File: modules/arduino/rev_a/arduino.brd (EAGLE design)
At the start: 67.3 x 66.7 mm, 45 parts, among them IC5 ATMEGA328P-20MU, J1 MODULE_GENERIC, J4 MICRO_USB_B_HIROSE_ZX62-B-5PA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, U3 ATMEGA8U2-MU, Y1 12 MHz, Y2 16MHz

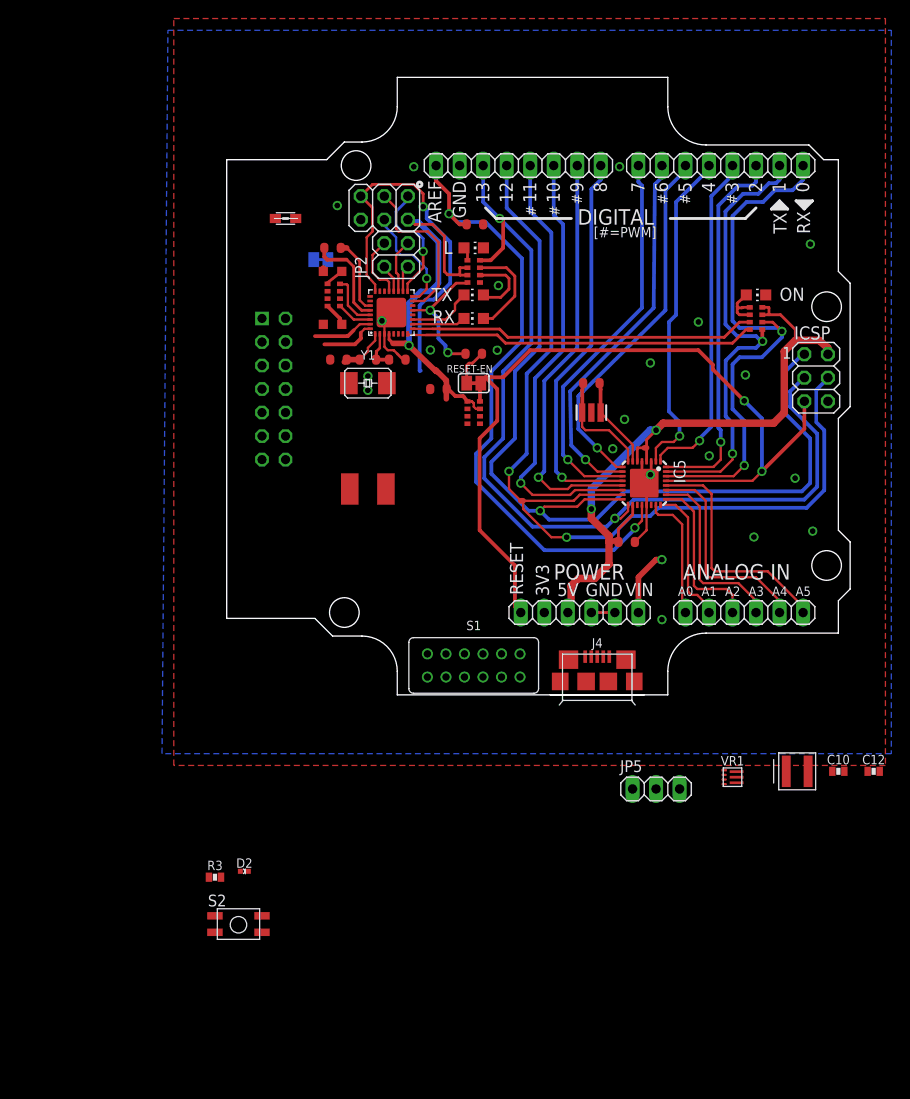
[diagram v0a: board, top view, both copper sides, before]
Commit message: Ardunio WIP
 - Add actual holes for signpost module mounts
 - Replace pin header with switch for IO voltage
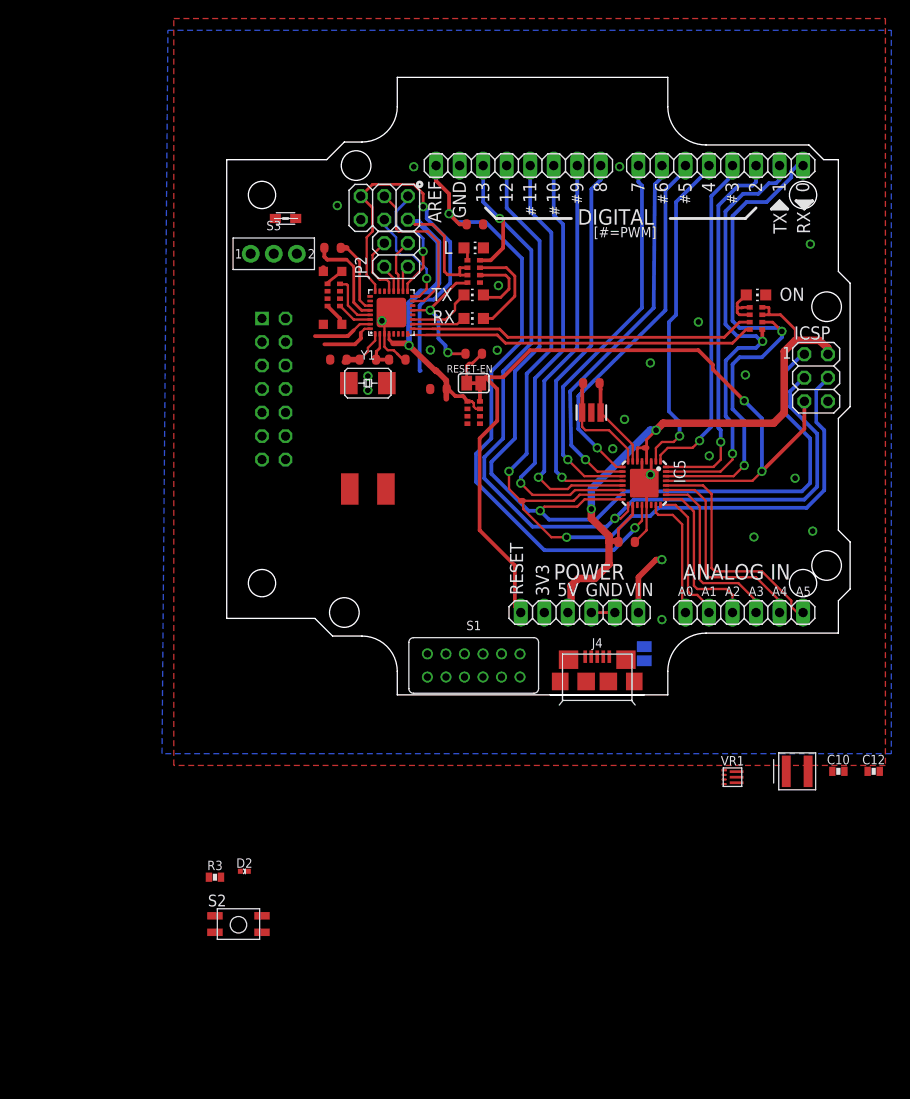
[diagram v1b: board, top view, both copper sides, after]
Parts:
- removed JP5: (no value), pinhead:1X03
- added S3: TE_SSA12/SPDT, switches:TE_SSA12/SPDT
- moved GROUND 55.0 mm to (46.4, -1.91), turned to 270 degrees
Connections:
- net +3V3: no longer JP5.3
- net +5V: now also S3.2
- net MOD_5V: no longer JP5.1
- net MOD_VCCIO: no longer JP5.2
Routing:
- net GND: track 22.2 -> 20.8 mm
- net IO0: track 58.0 -> 57.4 mm

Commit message: Not pretty but it's something
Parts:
- removed L1: BLM21, wuerth-elektronik:0805
- removed Z1, Z2: PGB1010604, varistor:CT/CN0603
- added D1: DIODE, passives:0402_DIODE
- added J2: (no value), jumper:SJ
- added LOGO1: UMICH_SOLID_MEDIUM, logos:UMICH_SOLID_200MIL
- moved C12 55.1 mm to (21.0, 8.26), turned to 270 degrees
- moved C10 54.2 mm to (18.4, 8.89)
- moved L2 51.7 mm to (19.4, 13.3)
- moved S2 50.3 mm to (32.4, 9.40), turned to 270 degrees
- moved VR1 42.9 mm to (18.4, 5.71), turned to 90 degrees
- moved D2 41.1 mm to (36.2, -0.95), turned to 90 degrees
- moved R3 34.3 mm to (19.1, 2.54)
- moved S3 29.2 mm to (6.35, 12.1)
- moved C8 4.51 mm to (15.1, 38.1)
- moved RN3 3.89 mm to (16.4, 35.2)
- moved C11 3.81 mm to (23.5, 29.8)
- moved C9 3.81 mm to (17.1, 29.8)
- moved R1 3.81 mm to (20.3, 29.8)
- moved Y1 3.81 mm to (20.3, 27.3)
- moved GROUND 2.69 mm to (48.3, 0.00), turned to 90 degrees
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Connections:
- net N$7 renamed VR_IND_SW
- removed net USHIELD: L1.2, Z1.2, Z2.2
- net +3V3: now also S3.1
- net +5V: now also C10.1, D1.CATHODE, VR1.1, VR1.7
- net ARD_USB_D+: now also RN3.7; no longer RN3.5, Z1.1
- net ARD_USB_D-: no longer Z2.1
- net ARD_USB_GND: no longer GROUND.2, L1.1
- net ARD_USB_VBUS: no longer D2.ANODE
- net EXT_USB_GND: now also GROUND.1
- net EXT_USB_VBUS: now also D2.ANODE
- net GND: now also GROUND.2; no longer GROUND.1
- net MOD_5V: now also D1.ANODE; no longer C10.1, VR1.1, VR1.7
- net MOD_IN: now also J2.1
- net MOD_VCCIO: now also S3.IN
- net RD+: now also RN3.2; no longer RN3.4
- net RESET: now also J2.2
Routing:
- net +5V: track 123.6 -> 192.8 mm, vias 3 -> 6
- net MOD_USB_VBUS: track 0.00 -> 53.1 mm
- net MOD_USB_D-: track 0.00 -> 51.7 mm
- net +3V3: track 0.00 -> 51.4 mm, vias 0 -> 1
- net ARD_USB_GND: track 10.5 -> 61.0 mm
- net MOD_USB_D+: track 0.00 -> 49.6 mm
- net ARD_USB_D-: track 2.56 -> 51.3 mm, vias 0 -> 1
- net ARD_USB_D+: track 2.14 -> 48.6 mm
- net ARD_USB_VBUS: track 0.00 -> 38.5 mm, vias 0 -> 3
- net EXT_USB_D-: track 0.00 -> 22.8 mm
- net MOD_VCCIO: track 0.00 -> 21.3 mm
- net EXT_USB_VBUS: track 0.00 -> 19.8 mm, vias 0 -> 2
- net USBVCC: track 6.49 -> 25.6 mm, vias 0 -> 2
- net EXT_USB_D+: track 0.00 -> 17.6 mm, vias 0 -> 1
- net RESET: track 98.4 -> 114.2 mm, vias 2 -> 6
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- added copper zone on layer 1, net +3V3
- added copper zone on layer 1, net +5V
- added copper zone on layer 16, net EXT_USB_GND
- added copper zone on layer 1, net VR_IND_SW
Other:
- outline, holes or cut-outs redrawn
- board text added: "2016-08-24"
- board text added: "Pat Pannuto"
- board text added: "Rev A"
- board text added: "Seinduino"

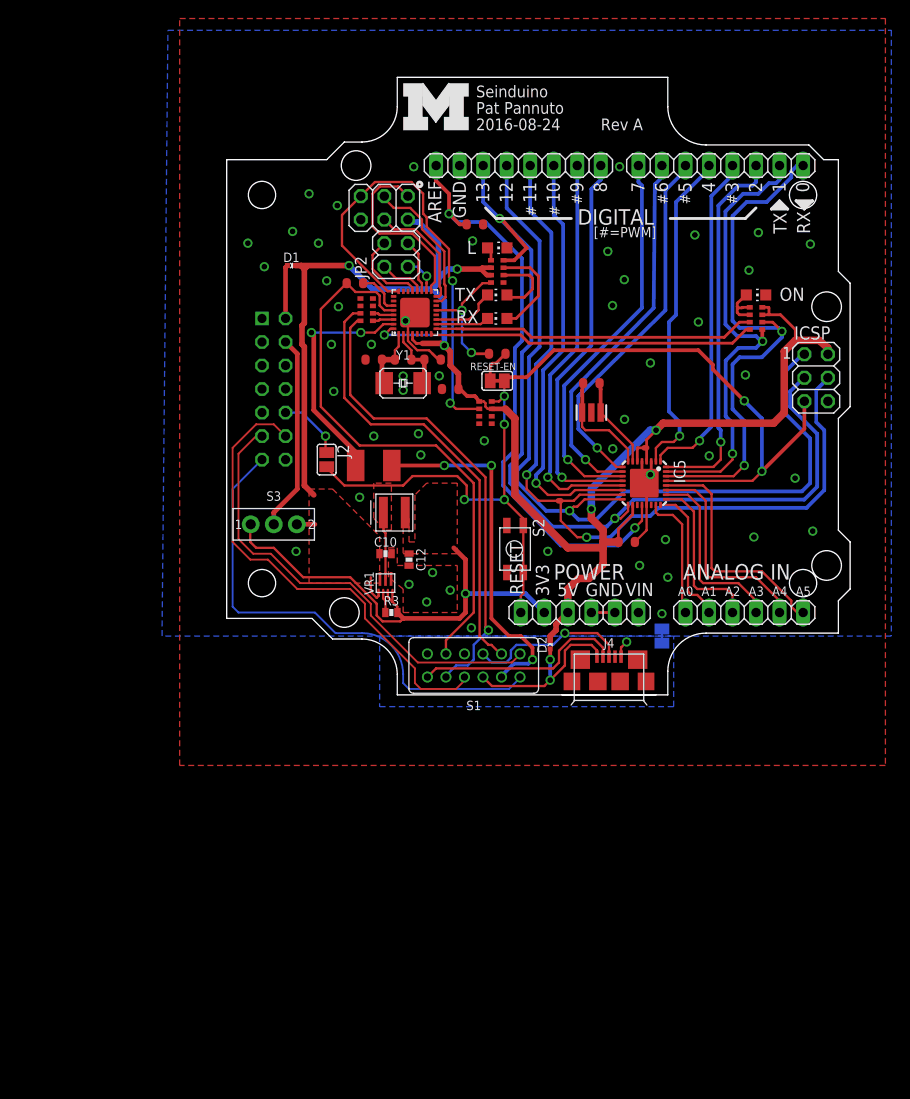
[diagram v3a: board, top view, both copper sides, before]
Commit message: Arduino: WIP, I should commit more frequently :(
The primary change in this commit is to extend the 3.3V/5V selection to the whole
board. The nice observation is that the two MCUs are 2.7-5.5 and 1.8-5.5 VCC tolerant,
so can do run-time selection of core voltage with a little bit of careful design. This
lets the seinduino look either like a Due (3.3V) or a Uno (5V).

The next mission is to replace that reset trigger circuit with a one-shot so that we
aren't cooking 5mA all the time.
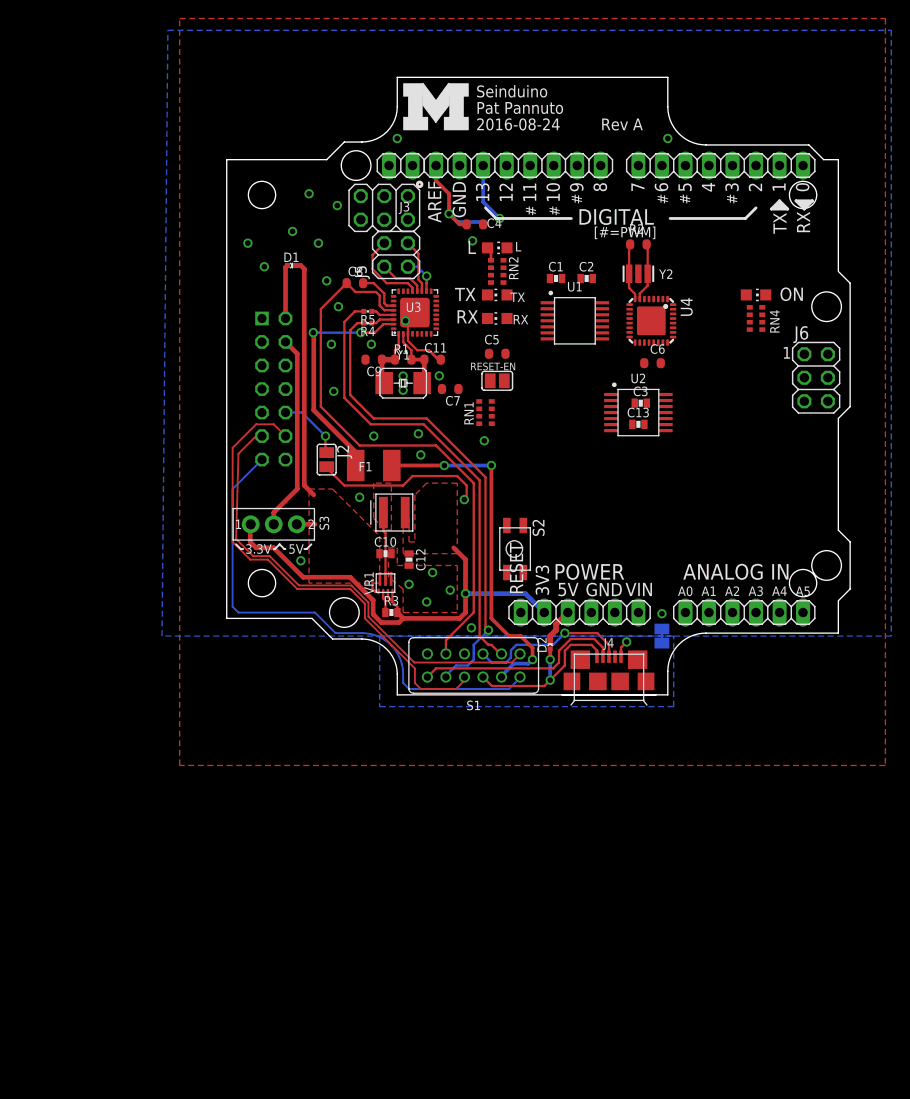
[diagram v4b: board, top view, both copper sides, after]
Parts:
- removed IC5: ATMEGA328P-20MU, idii:MLF32
- removed RN3: 22R, resistor-dil:CAY16
- added C1, C13, C2, C3: 100nF, passives:0603_CAP
- added JP1: (no value), pinhead:1X02
- added R4, R5: 22Ω, passives:0402_RES-HIGH_SPEED
- added U1, U2: ADG3304, chips:TSSOP-14/5MM
- added U4: ATMEGA328P-20MU, idii:MLF32
- C7: value 100n -> 100nF
- C8: value 1u -> 1uF
- J3: value ICSP -> ICSP_PROG
- moved C6 19.5 mm to (47.2, 29.5)
- moved Y2 15.8 mm to (45.7, 39.1)
- moved R2 15.8 mm to (45.7, 42.3)
- renumbered ICSP to J6, ICSP1 to J3, JP2 to J5
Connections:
- removed net EXT_USB_ID: J4.4
- removed net MISO2: J3.1, U3.17
- removed net MOD_VCCIO: J1.4, S3.IN
- removed net MOSI2: J3.4, U3.16
- removed net RD+: RN3.2, U3.29
- removed net RD-: RN3.1, U3.30
- removed net RESET2: J3.5, RN1.6, U3.24
- removed net SCK2: J3.3, U3.15
- new net ARD_USB_D+_TERM: R5.1, U3.29
- new net ARD_USB_D-_TERM: R4.1, U3.30
- new net MISO_PROG: U1.2, U3.17
- new net MISO_PROG_SHIFTED: J3.1, U1.13
- new net MISO_SHIFTED: J6.1, U2.13
- new net MOSI_PROG: U1.3, U3.16
- new net MOSI_PROG_SHIFTED: J3.4, U1.12
- new net MOSI_SHIFTED: J6.4, U2.12
- new net RESET_PROG: RN1.6, U1.5, U3.24
- new net RESET_PROG_SHIFTED: J3.5, U1.10
- new net RESET_SHIFTED: J6.5, U2.10
- new net SCK_PROG: U1.4, U3.15
- new net SCK_PROG_SHIFTED: J3.3, U1.11
- new net SCK_SHIFTED: J6.3, U2.11
- new net VCC: C13.2, C2.2, C6.2, C7.1, J1.4, RN1.3, RN1.5, S3.IN, U1.1, U1.8, U2.1, U2.8, U3.32, U3.4, U4.18, U4.4, U4.6
- net +5V: now also C1.1, C3.1, U1.14, U2.14; no longer C6.2, C7.1, IC5.18, IC5.4, IC5.6, RN1.3, RN1.5, U3.32, U3.4
- net AD0: now also U4.23; no longer IC5.23
- net AD1: now also U4.24; no longer IC5.24
- net AD2: now also U4.25; no longer IC5.25
- net AD3: now also U4.26; no longer IC5.26
- net AD4: now also JP1.2, U4.27; no longer IC5.27
- net AD5: now also JP1.1, U4.28; no longer IC5.28
- net ARD_USB_D+: now also R5.2; no longer RN3.7
- net ARD_USB_D-: now also R4.2; no longer RN3.8
- net AREF: now also U4.20; no longer IC5.20
- net GND: now also C1.2, C13.1, C2.1, C3.2, U1.7, U2.7, U4.21, U4.3, U4.5; no longer IC5.21, IC5.3, IC5.5
- net IO0: now also U4.30; no longer IC5.30
- net IO1: now also U4.31; no longer IC5.31
- net IO2: now also U4.32; no longer IC5.32
- net IO3: now also U4.1; no longer IC5.1
- net IO4: now also U4.2; no longer IC5.2
- net IO5: now also U4.9; no longer IC5.9
- net IO6: now also U4.10; no longer IC5.10
- net IO7: now also U4.11; no longer IC5.11
- net IO8: now also U4.12; no longer IC5.12
- net IO9: now also U4.13; no longer IC5.13
- net MISO: now also U2.2, U4.16; no longer IC5.16, J6.1
- net MOSI: now also U2.3, U4.15; no longer IC5.15, J6.4
- net RESET: now also U2.5, U4.29; no longer IC5.29, J6.5
- net SCK: now also U2.4, U4.17; no longer IC5.17, J6.3
- net SS: now also U4.14; no longer IC5.14
- net XTAL1: now also U4.7; no longer IC5.7
- net XTAL2: now also U4.8; no longer IC5.8
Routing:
- net +5V: track 192.8 -> 33.5 mm, vias 6 -> 0
- net RESET: track 114.2 -> 18.5 mm, vias 6 -> 1
- net MOSI: track 94.6 -> 0.00 mm, vias 2 -> 0
- net MISO: track 94.0 -> 0.00 mm, vias 1 -> 0
- net SCK: track 97.8 -> 6.45 mm, vias 2 -> 1
- net IO0: track 57.4 -> 0.00 mm, vias 2 -> 0
- net AREF: track 64.2 -> 12.5 mm, vias 2 -> 1
- net IO1: track 50.8 -> 0.00 mm, vias 2 -> 0
- net RESET2: track 49.7 -> 0.00 mm, vias 2 -> 0
- net SS: track 46.0 -> 0.00 mm, vias 1 -> 0
- net IO9: track 43.7 -> 0.00 mm, vias 1 -> 0
- net IO8: track 42.5 -> 0.00 mm, vias 1 -> 0
- net IO7: track 42.2 -> 0.00 mm, vias 1 -> 0
- net IO2: track 41.0 -> 0.00 mm, vias 1 -> 0
- net IO6: track 40.9 -> 0.00 mm, vias 1 -> 0
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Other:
- board text added: "3.3V"

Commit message: arudino: add reset network
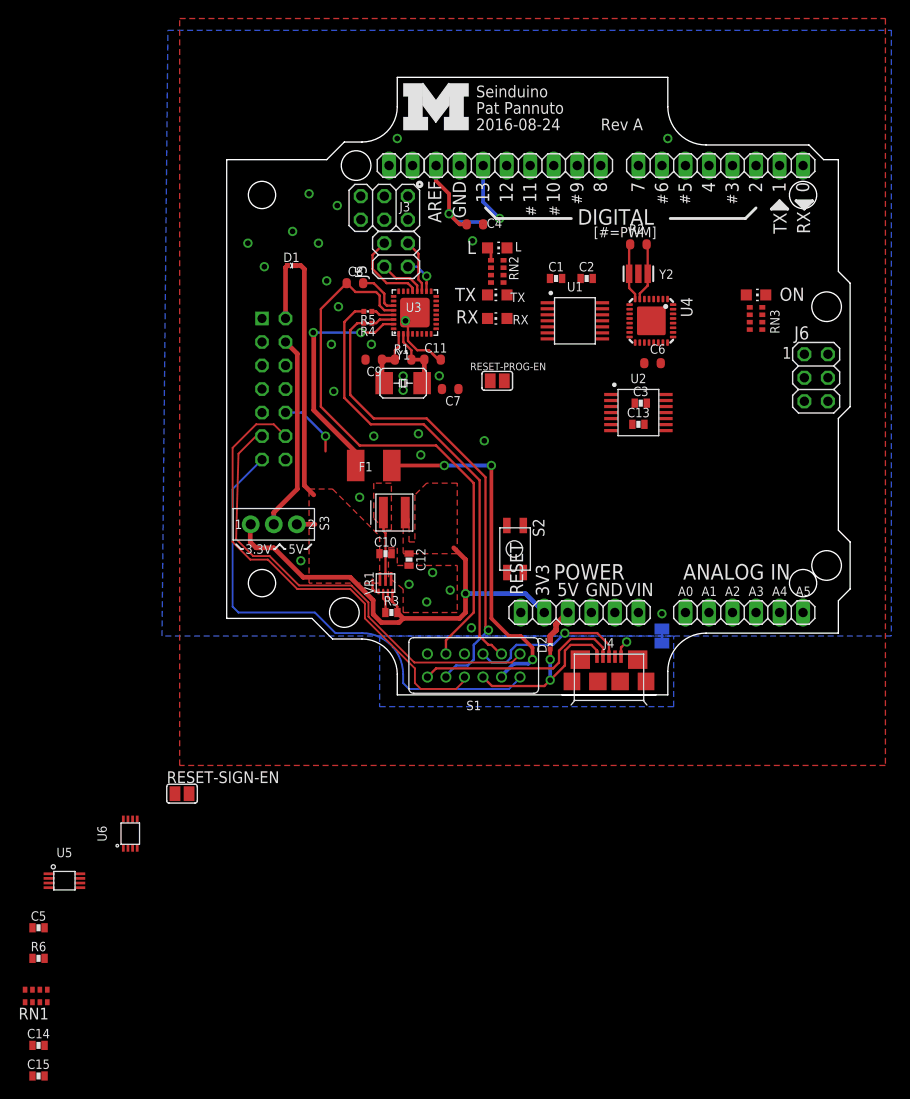
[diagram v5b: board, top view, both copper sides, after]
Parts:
- removed J2: (no value), jumper:SJ
- added C14, C15: 100nF, passives:0603_CAP
- added R6: 10kΩ, passives:0603-RES
- added RESET-SIGN-EN: (no value), jumper:SJ
- added U5: 74LVC2G00DC, chips:VSSOP-8
- added U6: SN74LVC1G123DCUR, chips:VFSOP-8
- C5: value 100n -> 100nF; device SmartPrj:C0603-ROUND -> passives:0603_CAP
- moved RN1 79.5 mm to (-19.3, -38.9), turned to 0 degrees
- moved C5 79.3 mm to (-19.1, -31.5)
- renumbered RESET-EN to RESET-PROG-EN, RN4 to RN3
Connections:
- removed net DTR: C5.1, RN2.4, U3.13
- new net DTR_PROG: RESET-PROG-EN.1, U3.13
- new net N$10: RESET-SIGN-EN.2, RN1.7, U5.2
- new net N$13: U5.5, U5.6, U6.5
- new net N$7: C5.2, RN1.3, U6.6
- new net N$8: U5.7, U6.1
- new net N$9: RESET-PROG-EN.2, RN1.8, U5.1
- net GND: now also C14.1, C15.1, RN1.6, U5.4, U6.4; no longer RN2.5
- net MOD_IN: now also RESET-SIGN-EN.1; no longer J2.1
- net RESET: now also RN1.5, U5.3; no longer C5.2, J2.2, RESET-PROG-EN.1, RESET-PROG-EN.2, RN1.4
- net RESET_PROG: now also R6.1; no longer RN1.6
- net VCC: now also C14.2, C15.2, C5.1, R6.2, RN1.1, RN1.2, RN1.4, U5.8, U6.2, U6.3, U6.7, U6.8; no longer RN1.3, RN1.5
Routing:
- net RESET: track 18.5 -> 0.00 mm, vias 1 -> 0
